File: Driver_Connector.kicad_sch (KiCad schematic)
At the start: 2 parts, among them J5 Driver, J6 Measurements

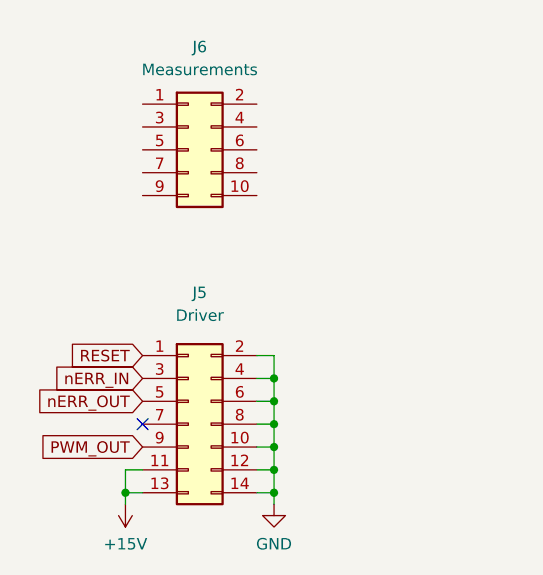
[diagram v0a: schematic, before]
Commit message: Добавил молексы и убрал питание
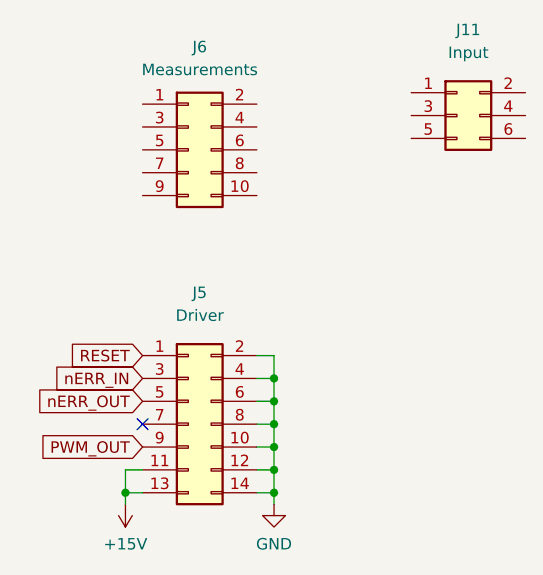
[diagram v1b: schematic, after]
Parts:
- added J11: Input, Connector_Molex:Molex_Micro-Fit_3.0_43045-0600_2x03_P3.00mm_Horizontal, symbol Connector_Generic:Conn_02x03_Odd_Even
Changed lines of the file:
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@@
     )
+  )
+  (symbol (lib_id "Connector_Generic:Conn_02x03_Odd_Even") (at 169.545 90.805 0) (unit 1)
+    (in_bom yes) (on_board yes) (fields_autoplaced)
+    (property "Reference" "J11" (id 0) (at 170.815 81.28 0))
+    (property "Value" "Input" (id 1) (at 170.815 83.82 0))
+    (property "Footprint" "Connector_Molex:Molex_Micro-Fit_3.0_43045-0600_2x03_P3.00mm_Horizontal" (id 2) (at 169.545 90.805 0)
+      (effects (font (size 1.27 1.27)) hide)
+    )
+    (property "Datasheet" "~" (id 3) (at 169.545 90.805 0)
+      (effects (font (size 1.27 1.27)) hide)
+    )
+    (pin "1")
+    (pin "2")
+    (pin "3")
+    (pin "4")
+    (pin "5")
+    (pin "6")
   )
   (symbol (lib_id "Connector_Generic:Conn_02x05_Odd_Even") (at 139.7 94.615 0) (unit 1)

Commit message: Первая версия в производство
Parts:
- removed J11: Input, Connector_Molex:Molex_Micro-Fit_3.0_43045-0600_2x03_P3.00mm_Horizontal, symbol Connector_Generic:Conn_02x03_Odd_Even
- removed J6: Measurements, Connector_IDC:IDC-Header_2x05_P2.54mm_Vertical, symbol Connector_Generic:Conn_02x05_Odd_Even

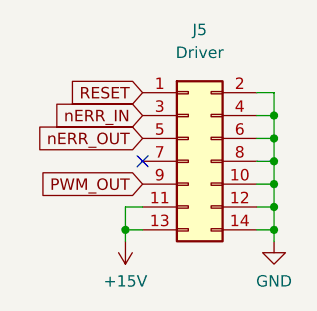
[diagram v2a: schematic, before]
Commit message: Добавил температуру, убрал подтяжки RS-485, заменил ШИМ на дифференциальный сигнал, добавил земли RS-485
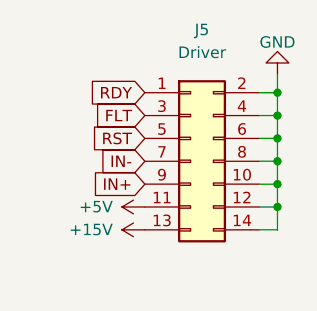
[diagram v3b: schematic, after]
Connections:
- net +15V: no longer J5.11 (Pin_11)
- net IN-: now reaches J5.7 (Pin_7)
- net PWM_OUT renamed IN+
- net RESET renamed RDY
- net nERR_IN renamed FLT
- net nERR_OUT renamed RST
- new net +5V: J5.11 (Pin_11)
- no-connect marks 1 -> 0
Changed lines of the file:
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@@
 (kicad_sch (version 20211123) (generator eeschema)
   (paper "A4")
-  (junction (at 132.715 132.842) (diameter 0) (color 0 0 0 0)
+  (junction (at 149.606 130.302) (diameter 0) (color 0 0 0 0)
   )
-  (junction (at 149.225 125.222) (diameter 0) (color 0 0 0 0)
+  (junction (at 149.606 117.602) (diameter 0) (color 0 0 0 0)
   )
-  (junction (at 149.225 130.302) (diameter 0) (color 0 0 0 0)
+  (junction (at 149.606 127.762) (diameter 0) (color 0 0 0 0)
   )
-  (junction (at 149.225 122.682) (diameter 0) (color 0 0 0 0)
+  (junction (at 149.606 122.682) (diameter 0) (color 0 0 0 0)
   )
-  (junction (at 149.225 132.842) (diameter 0) (color 0 0 0 0)
+  (junction (at 149.606 125.222) (diameter 0) (color 0 0 0 0)
   )
-  (junction (at 149.225 127.762) (diameter 0) (color 0 0 0 0)
+  (junction (at 149.606 120.142) (diameter 0) (color 0 0 0 0)
   )
-  (junction (at 149.225 120.142) (diameter 0) (color 0 0 0 0)
-  )
-  (no_connect (at 134.62 125.222))
-  (wire (pts (xy 147.32 120.142) (xy 149.225 120.142))
+  (wire (pts (xy 149.606 130.302) (xy 149.606 127.762))
     (stroke (width 0) (type default) (color 0 0 0 0))
   )
-  (wire (pts (xy 132.715 132.842) (xy 132.715 134.112))
+  (wire (pts (xy 147.574 132.842) (xy 149.606 132.842))
     (stroke (width 0) (type default) (color 0 0 0 0))
   )
-  (wire (pts (xy 149.225 125.222) (xy 149.225 127.762))
+  (wire (pts (xy 147.574 130.302) (xy 149.606 130.302))
     (stroke (width 0) (type default) (color 0 0 0 0))
   )
-  (wire (pts (xy 147.32 130.302) (xy 149.225 130.302))
+  (wire (pts (xy 149.606 122.682) (xy 149.606 120.142))
     (stroke (width 0) (type default) (color 0 0 0 0))
   )
-  (wire (pts (xy 147.32 125.222) (xy 149.225 125.222))
+  (wire (pts (xy 149.606 127.762) (xy 149.606 125.222))
     (stroke (width 0) (type default) (color 0 0 0 0))
   )
-  (wire (pts (xy 149.225 120.142) (xy 149.225 122.682))
+  (wire (pts (xy 149.606 125.222) (xy 149.606 122.682))
     (stroke (width 0) (type default) (color 0 0 0 0))
   )
-  (wire (pts (xy 132.715 130.302) (xy 132.715 132.842))
+  (wire (pts (xy 147.574 117.602) (xy 149.606 117.602))
     (stroke (width 0) (type default) (color 0 0 0 0))
   )
-  (wire (pts (xy 149.225 132.842) (xy 149.225 134.112))
+  (wire (pts (xy 147.574 122.682) (xy 149.606 122.682))
     (stroke (width 0) (type default) (color 0 0 0 0))
   )
-  (wire (pts (xy 147.32 127.762) (xy 149.225 127.762))
+  (wire (pts (xy 149.606 117.602) (xy 149.606 115.57))
     (stroke (width 0) (type default) (color 0 0 0 0))
   )
-  (wire (pts (xy 134.62 130.302) (xy 132.715 130.302))
+  (wire (pts (xy 149.606 132.842) (xy 149.606 130.302))
     (stroke (width 0) (type default) (color 0 0 0 0))
   )
-  (wire (pts (xy 149.225 122.682) (xy 149.225 125.222))
+  (wire (pts (xy 149.606 120.142) (xy 147.574 120.142))
     (stroke (width 0) (type default) (color 0 0 0 0))
   )
-  (wire (pts (xy 149.225 132.842) (xy 147.32 132.842))
+  (wire (pts (xy 147.574 127.762) (xy 149.606 127.762))
     (stroke (width 0) (type default) (color 0 0 0 0))
   )
-  (wire (pts (xy 149.225 127.762) (xy 149.225 130.302))
+  (wire (pts (xy 147.574 125.222) (xy 149.606 125.222))
     (stroke (width 0) (type default) (color 0 0 0 0))
   )
-  (wire (pts (xy 147.32 122.682) (xy 149.225 122.682))
+  (wire (pts (xy 149.606 117.602) (xy 149.606 120.142))
     (stroke (width 0) (type default) (color 0 0 0 0))
   )
-  (wire (pts (xy 147.32 117.602) (xy 149.225 117.602))
-    (stroke (width 0) (type default) (color 0 0 0 0))
-  )
-  (wire (pts (xy 132.715 132.842) (xy 134.62 132.842))
-    (stroke (width 0) (type default) (color 0 0 0 0))
-  )
-  (wire (pts (xy 149.225 130.302) (xy 149.225 132.842))
-    (stroke (width 0) (type default) (color 0 0 0 0))
-  )
-  (wire (pts (xy 149.225 117.602) (xy 149.225 120.142))
-    (stroke (width 0) (type default) (color 0 0 0 0))
-  )
-  (global_label "nERR_OUT" (shape input) (at 134.62 122.682 180) (fields_autoplaced)
+  (global_label "RST" (shape input) (at 134.874 122.682 180) (fields_autoplaced)
     (effects (font (size 1.27 1.27)) (justify right))
-    (property "Intersheet References" "${INTERSHEET_REFS}" (id 0) (at 122.7726 122.6026 0)
+    (property "Intersheet References" "${INTERSHEET_REFS}" (id 0) (at 129.0138 122.7614 0)
       (effects (font (size 1.27 1.27)) (justify right) hide)
     )
   )
-  (global_label "nERR_IN" (shape input) (at 134.62 120.142 180) (fields_autoplaced)
+  (global_label "IN-" (shape input) (at 134.874 125.222 180) (fields_autoplaced)
     (effects (font (size 1.27 1.27)) (justify right))
-    (property "Intersheet References" "${INTERSHEET_REFS}" (id 0) (at 124.4659 120.0626 0)
+    (property "Intersheet References" "${INTERSHEET_REFS}" (id 0) (at 128.9533 125.3014 0)
       (effects (font (size 1.27 1.27)) (justify right) hide)
     )
   )
-  (global_label "RESET" (shape input) (at 134.62 117.602 180) (fields_autoplaced)
+  (global_label "IN+" (shape input) (at 134.874 127.762 180) (fields_autoplaced)
     (effects (font (size 1.27 1.27)) (justify right))
-    (property "Intersheet References" "${INTERSHEET_REFS}" (id 0) (at 126.4617 117.5226 0)
+    (property "Intersheet References" "${INTERSHEET_REFS}" (id 0) (at 128.9533 127.8414 0)
       (effects (font (size 1.27 1.27)) (justify right) hide)
     )
   )
-  (global_label "PWM_OUT" (shape input) (at 134.62 127.762 180) (fields_autoplaced)
+  (global_label "RDY" (shape input) (at 134.874 117.602 180) (fields_autoplaced)
     (effects (font (size 1.27 1.27)) (justify right))
-    (property "Intersheet References" "${INTERSHEET_REFS}" (id 0) (at 123.4379 127.6826 0)
+    (property "Intersheet References" "${INTERSHEET_REFS}" (id 0) (at 128.8323 117.6814 0)
       (effects (font (size 1.27 1.27)) (justify right) hide)
     )
   )
-  (symbol (lib_id "power:GND") (at 149.225 134.112 0) (unit 1)
+  (global_label "FLT" (shape input) (at 134.874 120.142 180) (fields_autoplaced)
+    (effects (font (size 1.27 1.27)) (justify right))
+    (property "Intersheet References" "${INTERSHEET_REFS}" (id 0) (at 129.3766 120.2214 0)
+      (effects (font (size 1.27 1.27)) (justify right) hide)
+    )
+  )
+  (symbol (lib_id "power:+5V") (at 134.874 130.302 90) (unit 1)
     (in_bom yes) (on_board yes) (fields_autoplaced)
-    (property "Reference" "#PWR014" (id 0) (at 149.225 140.462 0)
+    (property "Reference" "#PWR054" (id 0) (at 138.684 130.302 0)
       (effects (font (size 1.27 1.27)) hide)
     )
-    (property "Value" "GND" (id 1) (at 149.225 138.557 0))
-    (property "Footprint" "" (id 2) (at 149.225 134.112 0)
+    (property "Value" "+5V" (id 1) (at 131.318 130.3021 90)
+      (effects (font (size 1.27 1.27)) (justify left))
+    )
+    (property "Footprint" "" (id 2) (at 134.874 130.302 0)
       (effects (font (size 1.27 1.27)) hide)
     )
-    (property "Datasheet" "" (id 3) (at 149.225 134.112 0)
+    (property "Datasheet" "" (id 3) (at 134.874 130.302 0)
       (effects (font (size 1.27 1.27)) hide)
     )
     (pin "1")
   )
-  (symbol (lib_id "power:+15V") (at 132.715 134.112 180) (unit 1)
+  (symbol (lib_id "power:+15V") (at 134.874 132.842 90) (unit 1)
     (in_bom yes) (on_board yes) (fields_autoplaced)
-    (property "Reference" "#PWR013" (id 0) (at 132.715 130.302 0)
+    (property "Reference" "#PWR046" (id 0) (at 138.684 132.842 0)
       (effects (font (size 1.27 1.27)) hide)
     )
-    (property "Value" "+15V" (id 1) (at 132.715 138.557 0))
-    (property "Footprint" "" (id 2) (at 132.715 134.112 0)
+    (property "Value" "+15V" (id 1) (at 131.318 132.8421 90)
+      (effects (font (size 1.27 1.27)) (justify left))
+    )
+    (property "Footprint" "" (id 2) (at 134.874 132.842 0)
       (effects (font (size 1.27 1.27)) hide)
     )
-    (property "Datasheet" "" (id 3) (at 132.715 134.112 0)
+    (property "Datasheet" "" (id 3) (at 134.874 132.842 0)
       (effects (font (size 1.27 1.27)) hide)
     )
     (pin "1")
   )
-  (symbol (lib_id "Connector_Generic:Conn_02x07_Odd_Even") (at 139.7 125.222 0) (unit 1)
-    (in_bom yes) (on_board yes) (fields_autoplaced)
-    (property "Reference" "J5" (id 0) (at 140.97 110.617 0))
-    (property "Value" "Driver" (id 1) (at 140.97 113.157 0))
-    (property "Footprint" "Connector_IDC:IDC-Header_2x07-1MP_P2.54mm_Latch_Vertical" (id 2) (at 139.7 125.222 0)
+  (symbol (lib_id "power:GND") (at 149.606 115.57 180) (unit 1)
+    (in_bom yes) (on_board yes)
+    (property "Reference" "#PWR014" (id 0) (at 149.606 109.22 0)
       (effects (font (size 1.27 1.27)) hide)
     )
-    (property "Datasheet" "~" (id 3) (at 139.7 125.222 0)
+    (property "Value" "GND" (id 1) (at 149.606 112.014 0))
+    (property "Footprint" "" (id 2) (at 149.606 115.57 0)
       (effects (font (size 1.27 1.27)) hide)
     )
+    (property "Datasheet" "" (id 3) (at 149.606 115.57 0)
+      (effects (font (size 1.27 1.27)) hide)
+    )
+    (pin "1")
+  )
+  (symbol (lib_id "Connector_Generic:Conn_02x07_Odd_Even") (at 139.954 125.222 0) (unit 1)
+    (in_bom yes) (on_board yes) (fields_autoplaced)
+    (property "Reference" "J5" (id 0) (at 141.224 110.617 0))
+    (property "Value" "Driver" (id 1) (at 141.224 113.157 0))
+    (property "Footprint" "Connector_IDC:IDC-Header_2x07-1MP_P2.54mm_Latch_Vertical" (id 2) (at 139.954 125.222 0)
+      (effects (font (size 1.27 1.27)) hide)
+    )
+    (property "Datasheet" "~" (id 3) (at 139.954 125.222 0)
+      (effects (font (size 1.27 1.27)) hide)
+    )
